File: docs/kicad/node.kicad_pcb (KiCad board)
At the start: 2 copper layers, 15 parts, among them J1 Conn_01x01_Pin, J2 Conn_01x01_Pin, J3 Conn_01x01_Pin, J4 Conn_01x01_Pin, J5 Conn_01x01_Pin, J6 Conn_01x01_Pin, J7 Conn_01x01_Pin, J8 Conn_01x01_Pin, J9 Conn_01x08, U1 ESP32-DevKitC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

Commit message: nit
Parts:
- moved U5 63.0 mm to (104.5, 136.5), turned to -90 degrees
- moved J9 49.7 mm to (51.0, 144.6), turned to 0 degrees

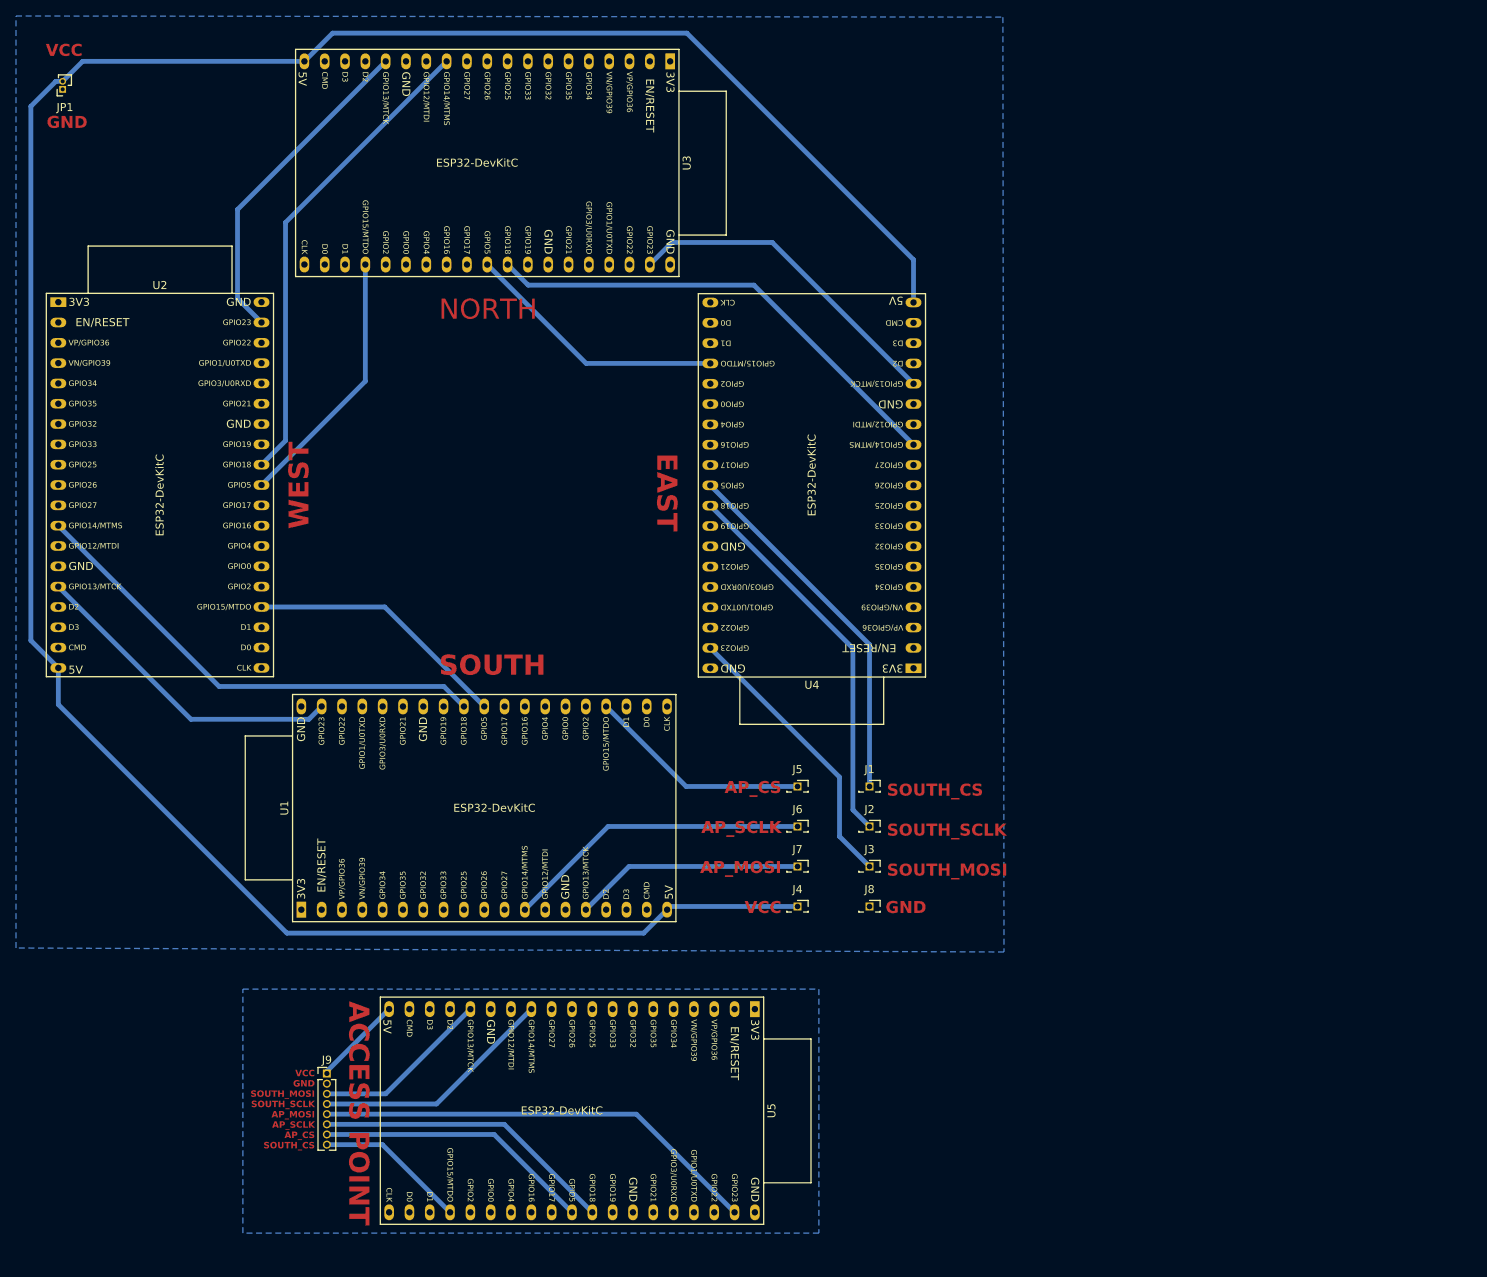
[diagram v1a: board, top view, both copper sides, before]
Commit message: fixed all DRC errors/warnings
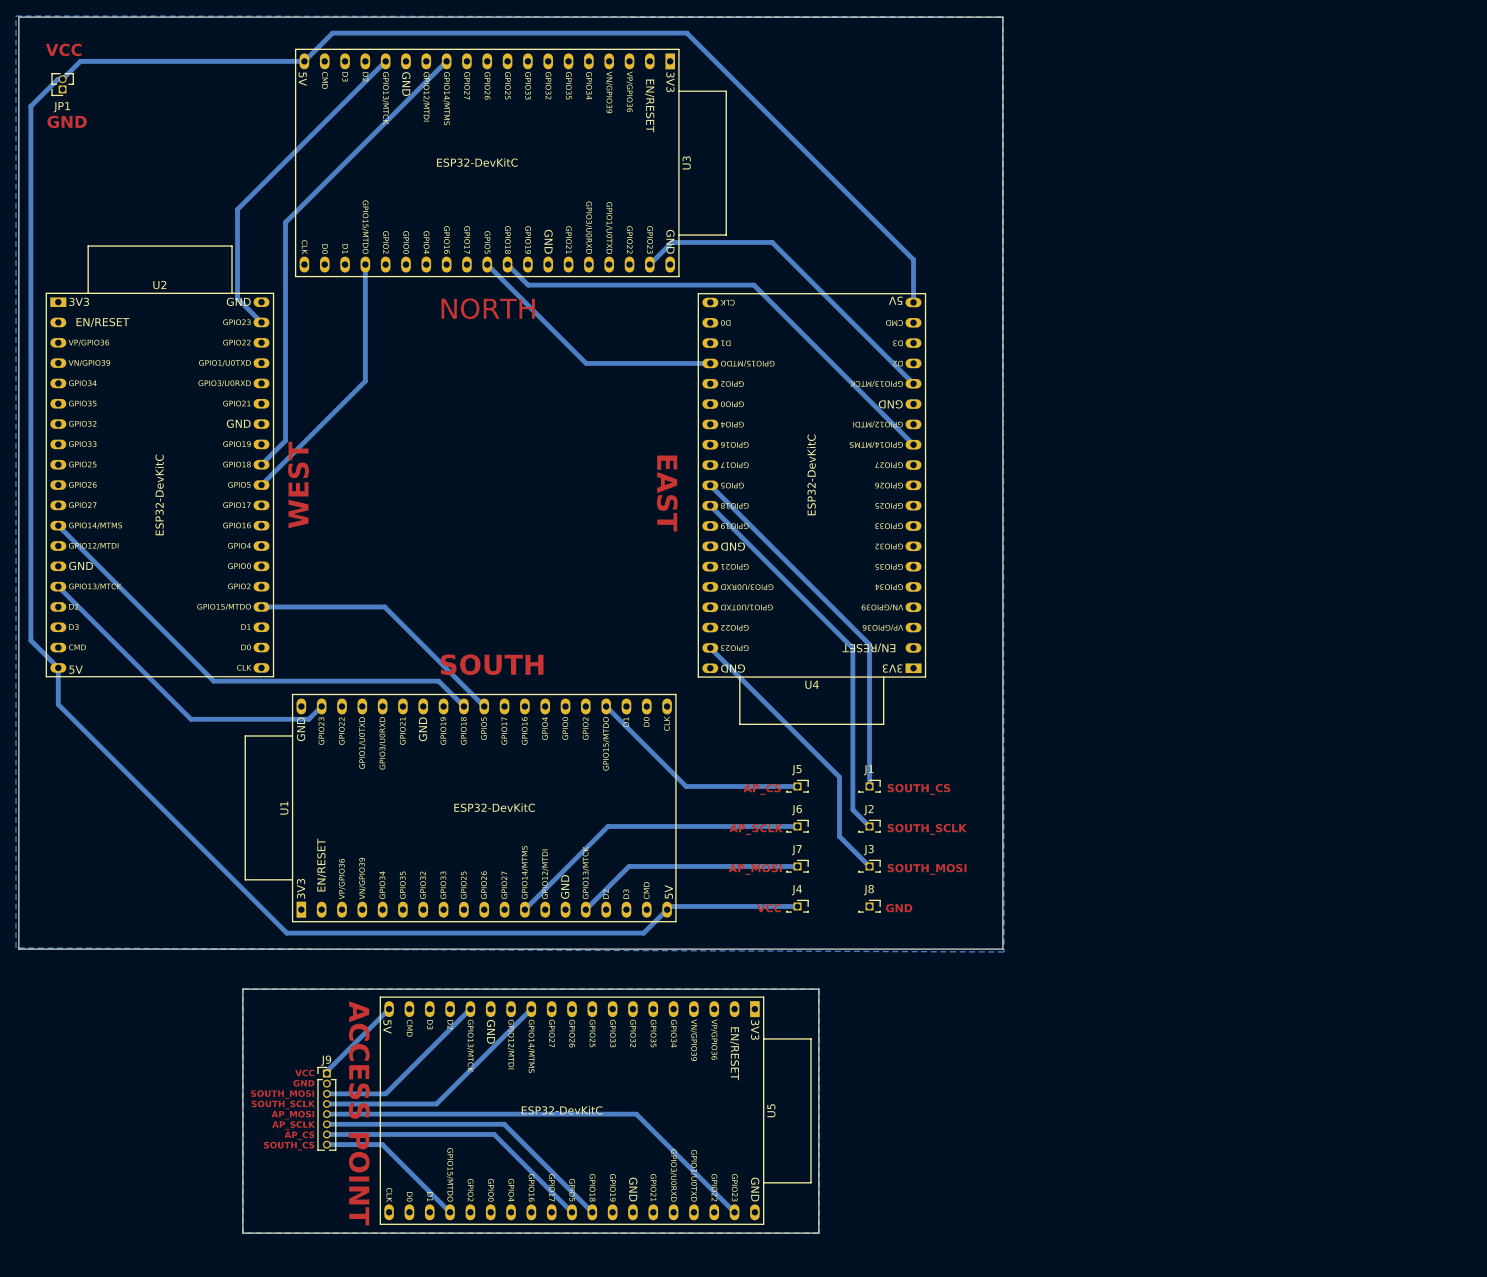
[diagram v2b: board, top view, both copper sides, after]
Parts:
- JP1: footprint Connector_PinSocket_1.00mm:PinSocket_1x02_P1.00mm_Vertical -> Connector_PinSocket_1.27mm:PinSocket_1x02_P1.27mm_Vertical
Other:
- board outline added: 123 x 152 mm

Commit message: nit
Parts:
- moved J1 3.67 mm to (122.5, 108.7)
- moved J2 3.67 mm to (122.5, 113.7)
- moved J3 3.67 mm to (122.5, 118.7)
- moved J4 3.67 mm to (113.5, 123.7)
- moved J5 3.67 mm to (113.5, 108.7)
- moved J6 3.67 mm to (113.5, 113.7)
- moved J7 3.67 mm to (113.5, 118.7)
- moved J8 3.67 mm to (122.5, 123.7)
- moved JP1 3.67 mm to (21.6, 21.5)
- moved U2 3.67 mm to (21.1, 48.1)
- moved U3 3.67 mm to (97.6, 18.0)
- moved U4 3.67 mm to (128.0, 93.9)
- moved U1 3.67 mm to (51.5, 124.1)

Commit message: nit
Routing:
- net GND1: track 0.00 -> 46.3 mm
- net GND: track 0.00 -> 32.0 mm
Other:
- board size 123 x 152 mm -> 123 x 153 mm
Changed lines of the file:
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@@
 	)
 	(gr_rect
-		(start 40.5 134)
-		(end 112.5 164.5)
+		(start 40.5 133)
+		(end 112.5 165.5)
 		(stroke
 			(width 0.05)
@@
 	)
 	(segment
+		(start 56.56 100.06)
+		(end 56.56 98.67)
+		(width 1.5)
+		(layer "B.Cu")
+		(net 1)
+	)
+	(segment
+		(start 43 55.5)
+		(end 45.29 53.21)
+		(width 1.5)
+		(layer "B.Cu")
+		(net 1)
+	)
+	(segment
+		(start 43 59)
+		(end 43 55.5)
+		(width 1.5)
+		(layer "B.Cu")
+		(net 1)
+	)
+	(segment
+		(start 44.83 60.83)
+		(end 43 59)
+		(width 1.5)
+		(layer "B.Cu")
+		(net 1)
+	)
+	(segment
+		(start 66.72 100.28)
+		(end 65 102)
+		(width 1.5)
+		(layer "B.Cu")
+		(net 1)
+	)
+	(segment
+		(start 65 102)
+		(end 58.5 102)
+		(width 1.5)
+		(layer "B.Cu")
+		(net 1)
+	)
+	(segment
+		(start 102.6 78.65)
+		(end 102.6 81.19)
+		(width 1.5)
+		(layer "B.Cu")
+		(net 1)
+	)
+	(segment
+		(start 46.5 63.37)
+		(end 46.5 60.83)
+		(width 1.5)
+		(layer "B.Cu")
+		(net 1)
+	)
+	(segment
+		(start 45.29 53.21)
+		(end 46.5 53.21)
+		(width 1.5)
+		(layer "B.Cu")
+		(net 1)
+	)
+	(segment
+		(start 58.5 102)
+		(end 56.56 100.06)
+		(width 1.5)
+		(layer "B.Cu")
+		(net 1)
+	)
+	(segment
+		(start 66.72 98.67)
+		(end 66.72 100.28)
+		(width 1.5)
+		(layer "B.Cu")
+		(net 1)
+	)
+	(segment
+		(start 46.5 60.83)
+		(end 44.83 60.83)
+		(width 1.5)
+		(layer "B.Cu")
+		(net 1)
+	)
+	(segment
 		(start 97.6 123.67)
 		(end 97.2 124.07)
@@
 	)
 	(segment
-		(start 49.5 38.17)
-		(end 49.5 65.45)
+		(start 50 38.254365)
+		(end 69.64 18.614365)
 		(width 0.6)
 		(layer "B.Cu")
@@
 	)
 	(segment
-		(start 49.5 65.45)
-		(end 46.5 68.45)
+		(start 46.5 68.45)
+		(end 50 64.95)
 		(width 0.6)
 		(layer "B.Cu")
@@
 	)
 	(segment
-		(start 69.64 18.03)
-		(end 49.5 38.17)
+		(start 69.64 18.614365)
+		(end 69.64 18.03)
+		(width 0.6)
+		(layer "B.Cu")
+		(net 67)
+	)
+	(segment
+		(start 50 64.95)
+		(end 50 38.254365)
 		(width 0.6)
 		(layer "B.Cu")
@@
 		(net 132)
 	)
+	(segment
+		(start 50 142)
+		(end 57.5 134.5)
+		(width 0.6)
+		(layer "B.Cu")
+		(net 160)
+	)
+	(segment
+		(start 77.25 164.25)
+		(end 88 164.25)
+		(width 1.5)
+		(layer "B.Cu")
+		(net 160)
+	)
+	(segment
+		(start 69.48 134.5)
+		(end 71.48 136.5)
+		(width 0.6)
+		(layer "B.Cu")
+		(net 160)
+	)
+	(segment
+		(start 57.5 134.5)
+		(end 69.48 134.5)
+		(width 0.6)
+		(layer "B.Cu")
+		(net 160)
+	)
+	(segment
+		(start 50 145.55)
+		(end 50 142)
+		(width 0.6)
+		(layer "B.Cu")
+		(net 160)
+	)
+	(segment
+		(start 76.56 161.9)
+		(end 76.56 163.56)
+		(width 1.5)
+		(layer "B.Cu")
+		(net 160)
+	)
+	(segment
+		(start 50.27 145.82)
+		(end 50 145.55)
+		(width 0.6)
+		(layer "B.Cu")
+		(net 160)
+	)
+	(segment
+		(start 88 164.25)
+		(end 89.26 162.99)
+		(width 1.5)
+		(layer "B.Cu")
+		(net 160)
+	)
+	(segment
+		(start 89.26 162.99)
+		(end 89.26 161.9)
+		(width 1.5)
+		(layer "B.Cu")
+		(net 160)
+	)
+	(segment
+		(start 76.56 163.56)
+		(end 77.25 164.25)
+		(width 1.5)
+		(layer "B.Cu")
+		(net 160)
+	)
+	(segment
+		(start 51 145.82)
+		(end 50.27 145.82)
+		(width 0.6)
+		(layer "B.Cu")
+		(net 160)
+	)
 	(zone
 		(net 1)
 		(net_name "GND")
 		(layer "B.Cu")
+		(hatch edge 0.6)
+		(connect_pads
+			(clearance 0.6)
+		)
+		(min_thickness 0.25)
+		(filled_areas_thickness no)
+		(fill yes
+			(thermal_gap 0.4)
+			(thermal_bridge_width 0.5)
+		)
+		(polygon
+			(pts
+				(xy 12.14 12.36) (xy 135.5 12.5) (xy 135.64 129.36) (xy 12.14 128.86)
+			)
+		)
+	)
+	(zone
+		(net 160)
+		(net_name "GND1")
+		(layer "B.Cu")
 		(hatch edge 0.5)
+		(priority 1)
 		(connect_pads
 			(clearance 0.5)
@@
 		(polygon
 			(pts
-				(xy 12.14 12.36) (xy 135.5 12.5) (xy 135.64 129.36) (xy 12.14 128.86)
-			)
-		)
-	)
-	(zone
-		(net 160)
-		(net_name "GND1")
-		(layer "B.Cu")
-		(hatch edge 0.5)
-		(priority 1)
-		(connect_pads
-			(clearance 0.5)
-		)
-		(min_thickness 0.25)
-		(filled_areas_thickness no)
-		(fill yes
-			(thermal_gap 0.5)
-			(thermal_bridge_width 0.5)
-		)
-		(polygon
-			(pts
-				(xy 112.5 164.5) (xy 40.5 164.5) (xy 40.5 134) (xy 112.5 134)
-			)
-		)
+				(xy 112.5 165.5) (xy 40.5 165.5) (xy 40.5 133) (xy 112.5 133)
+			)
+		)

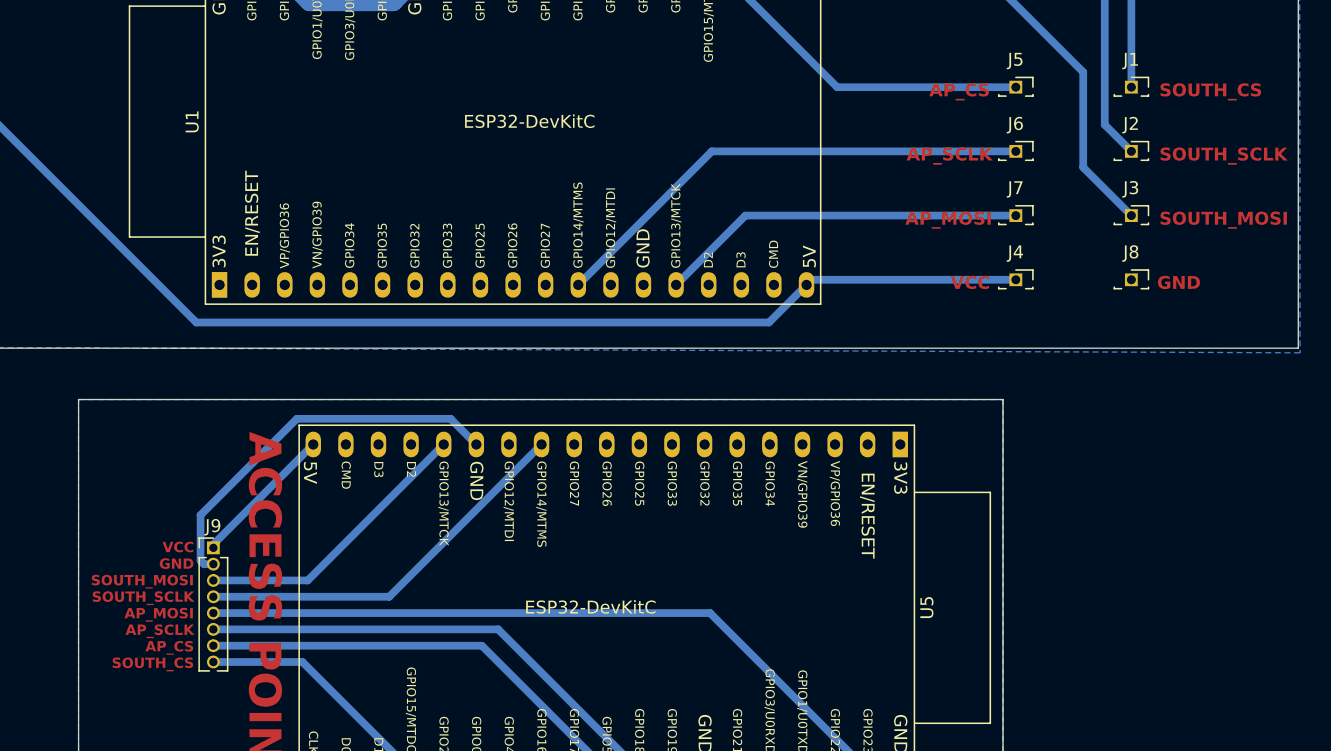
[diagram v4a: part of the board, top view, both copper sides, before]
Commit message: updated labels
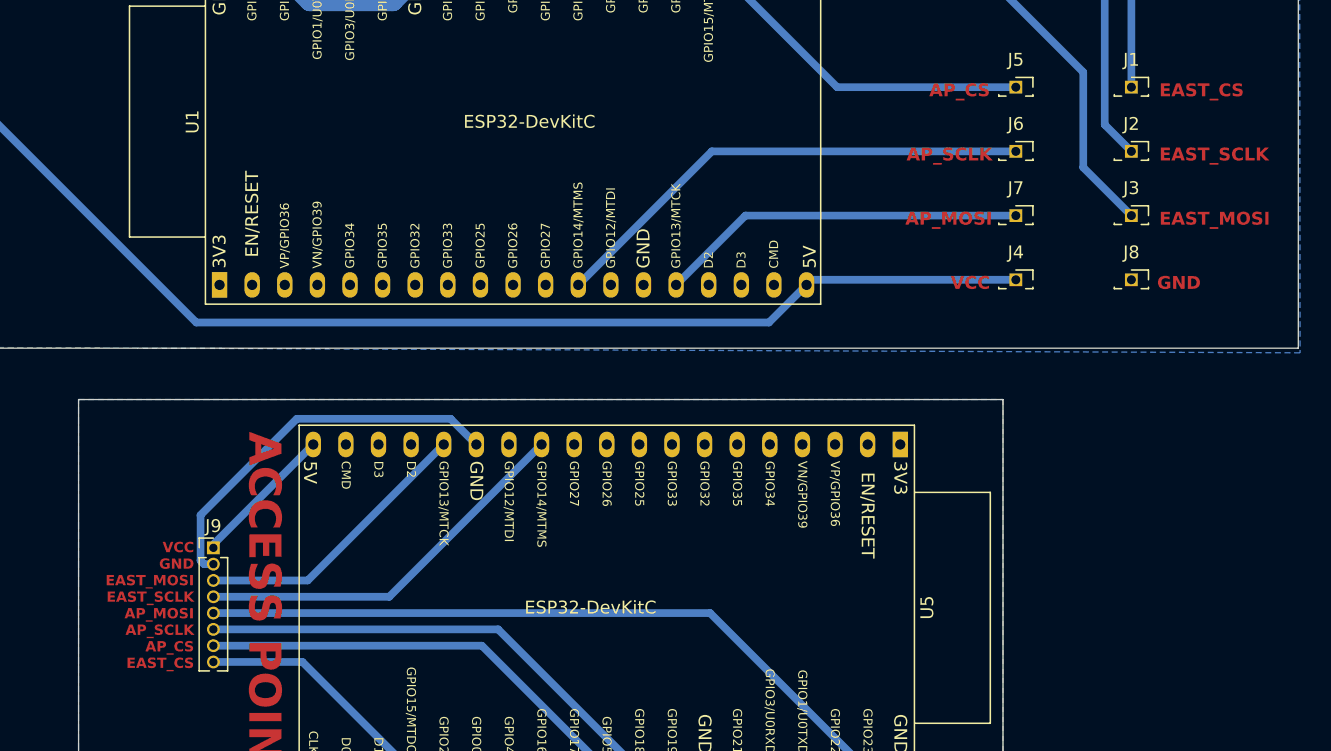
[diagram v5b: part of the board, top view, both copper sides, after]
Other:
- board text added: "EAST_CS"
- board text added: "EAST_MOSI"
- board text added: "EAST_SCLK"
- board text added: "VCC GND EAST_MOSI EAST_SCLK AP_MOSI AP_SCLK AP_CS EAST_CS"
- board text removed: "SOUTH_CS"
- board text removed: "SOUTH_MOSI"
- board text removed: "SOUTH_SCLK"
- board text removed: "VCC GND SOUTH_MOSI SOUTH_SCLK AP_MOSI AP_SCLK AP_CS SOUTH_CS"
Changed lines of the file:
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@@
 		)
 	)
-	(gr_text "SOUTH_CS"
+	(gr_text "EAST_CS"
 		(at 124.67 109.5 0)
 		(layer "F.Cu")
@@
 		)
 	)
-	(gr_text "VCC\nGND\nSOUTH_MOSI\nSOUTH_SCLK\nAP_MOSI\nAP_SCLK\nAP_CS\nSOUTH_CS"
+	(gr_text "VCC\nGND\nEAST_MOSI\nEAST_SCLK\nAP_MOSI\nAP_SCLK\nAP_CS\nEAST_CS"
 		(at 49.5 154 0)
 		(layer "F.Cu")
@@
 		)
 	)
-	(gr_text "SOUTH_SCLK"
+	(gr_text "EAST_SCLK"
 		(at 124.67 114.5 0)
 		(layer "F.Cu")
@@
 		)
 	)
-	(gr_text "SOUTH_MOSI"
+	(gr_text "EAST_MOSI"
 		(at 124.67 119.5 0)
 		(layer "F.Cu")
